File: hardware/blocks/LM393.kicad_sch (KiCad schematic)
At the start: 20 parts, among them J5 Conn_01x02/DIN, U3 LM393

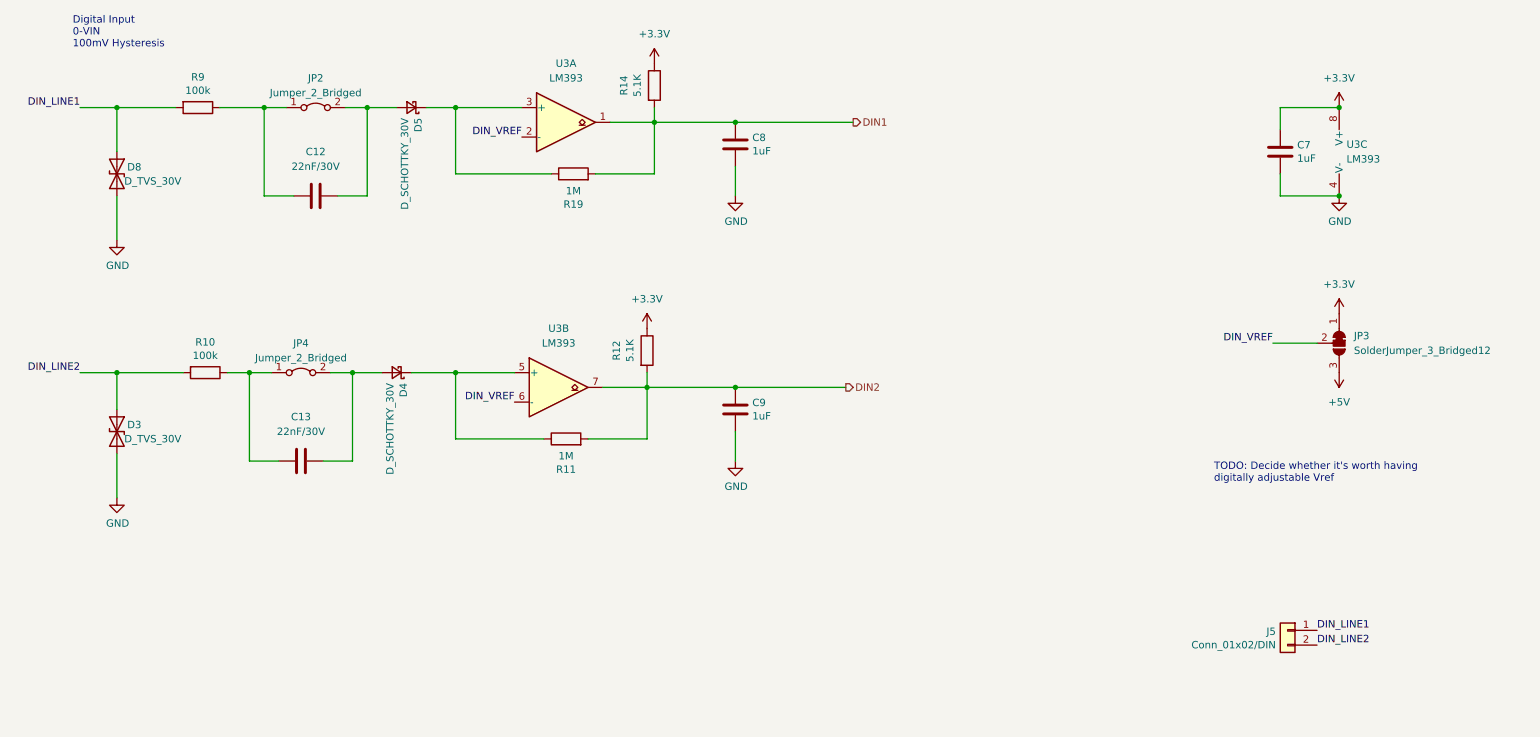
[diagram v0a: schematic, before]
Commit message: Added 3D models and ran freerouting
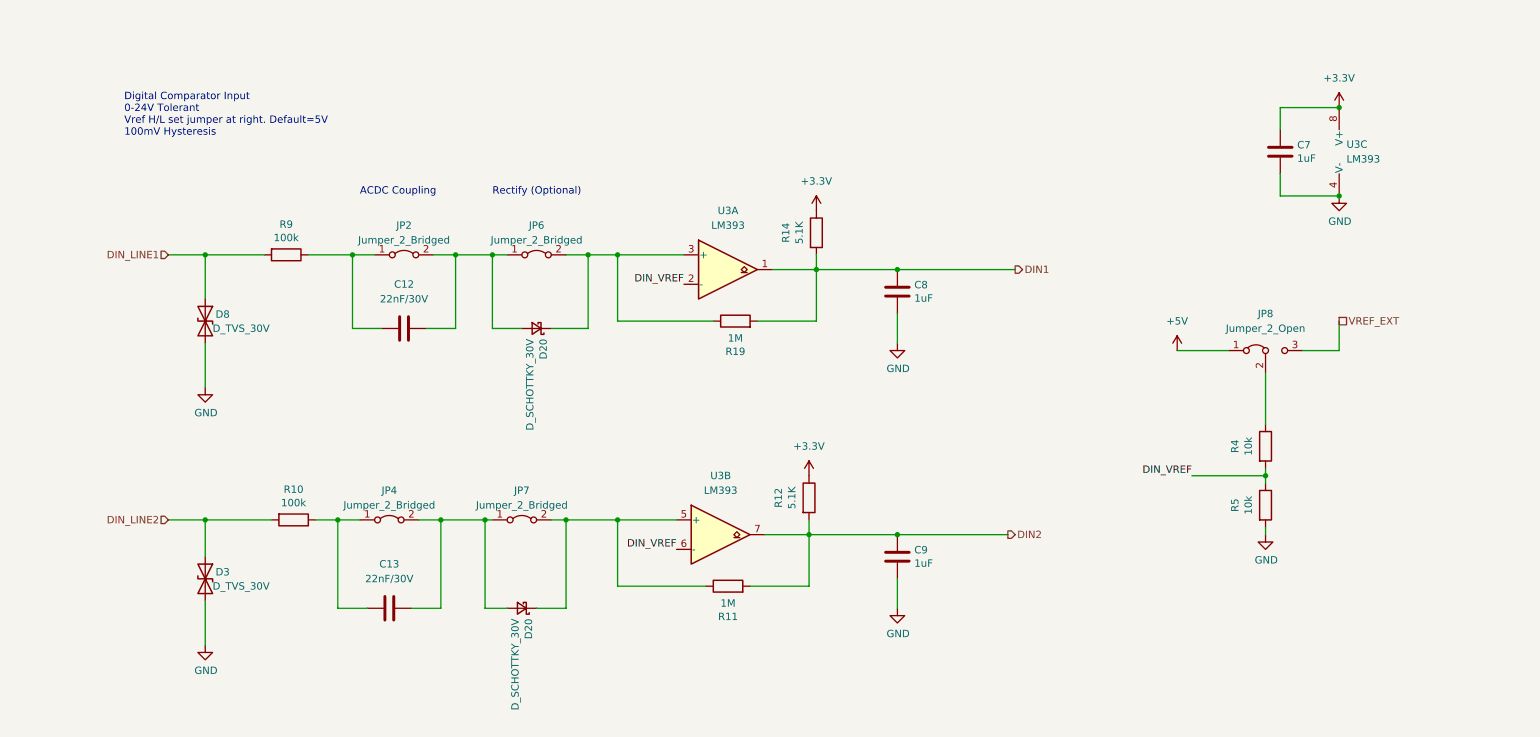
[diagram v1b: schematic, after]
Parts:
- removed D4, D5: D_SCHOTTKY_30V, Diode_SMD:D_SOD-123, symbol Device:D_Schottky_Small
- removed J5: Conn_01x02/DIN, TerminalBlock:TerminalBlock_Altech_AK300-2_P5.00mm, symbol Connector_Generic:Conn_01x02
- removed JP3: SolderJumper_3_Bridged12, Jumper:SolderJumper-3_P1.3mm_Bridged12_Pad1.0x1.5mm_NumberLabels, symbol Jumper:SolderJumper_3_Bridged12
- added D20 (x2): D_SCHOTTKY_30V, Diode_SMD:D_SOD-123, symbol Device:D_Schottky_Small
- added JP6, JP7: Jumper_2_Bridged, Connector_PinHeader_2.54mm:PinHeader_1x02_P2.54mm_Vertical, symbol Jumper:Jumper_2_Bridged
- added JP8: Jumper_2_Open, Connector_PinHeader_2.54mm:PinHeader_1x03_P2.54mm_Vertical, symbol Jumper:Jumper_3_Bridged12
- added R4, R5: 10k, Resistor_SMD:R_0805_2012Metric, symbol Device:R
- C12, C13, C7, C8, C9: footprint Capacitor_SMD:C_0603_1608Metric -> Capacitor_SMD:C_0805_2012Metric
- JP2, JP4: footprint Connector_PinHeader_1.00mm:PinHeader_1x02_P1.00mm_Vertical -> Connector_PinHeader_2.54mm:PinHeader_1x02_P2.54mm_Vertical
- R10, R11, R12, R14, R19, R9: footprint Resistor_SMD:R_0603_1608Metric -> Resistor_SMD:R_0805_2012Metric
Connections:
- net +5V: now also JP8.1 (A)
- net DIN_VREF: now also R4.2, R5.1
- net GND: now also R5.2
- net at C13.1, JP4.2 (B): now also D20.2 (A), JP7.1 (A)
- net at R11.1, U3.5 (+): now also D20.1 (K), JP7.2 (B)
- net at R19.1, U3.3 (+): now also D20.1 (K), JP6.2 (B)
- net at C12.1, JP2.2 (B): now also D20.2 (A), JP6.1 (A)
- new net: JP8.2 (C), R4.1
- new net VREF_EXT: JP8.3 (B)
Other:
- note added: "ACDC Coupling"
- note added: "Digital Comparator Input 0-24V Tolerant Vref H/L set jumper at right. Default=5V 100mV Hysteresis"
- note added: "Rectify (Optional)"
- note removed: "Digital Input 0-VIN 100mV Hysteresis"
- note removed: "TODO: Decide whether it's worth having digitally adjustable Vref"
- moved on the sheet: C12, C13, C8, C9, D3, D8, JP2, JP4, R10, R11, R12, R14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
